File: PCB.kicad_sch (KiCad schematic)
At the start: 17 parts, among them J1 Conector IR, J10 Conector ultrassonico esquerdo, J11 Conector ultrassonico central, J12 Conector ultrassonico direito, J13 Conector LED Extra, J14 Conector LORA, J15 ENCO_SW_Esq, J16 ENCO_SW_Dir, J2 Conector bluetooth, J3 Conector Acelerometro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

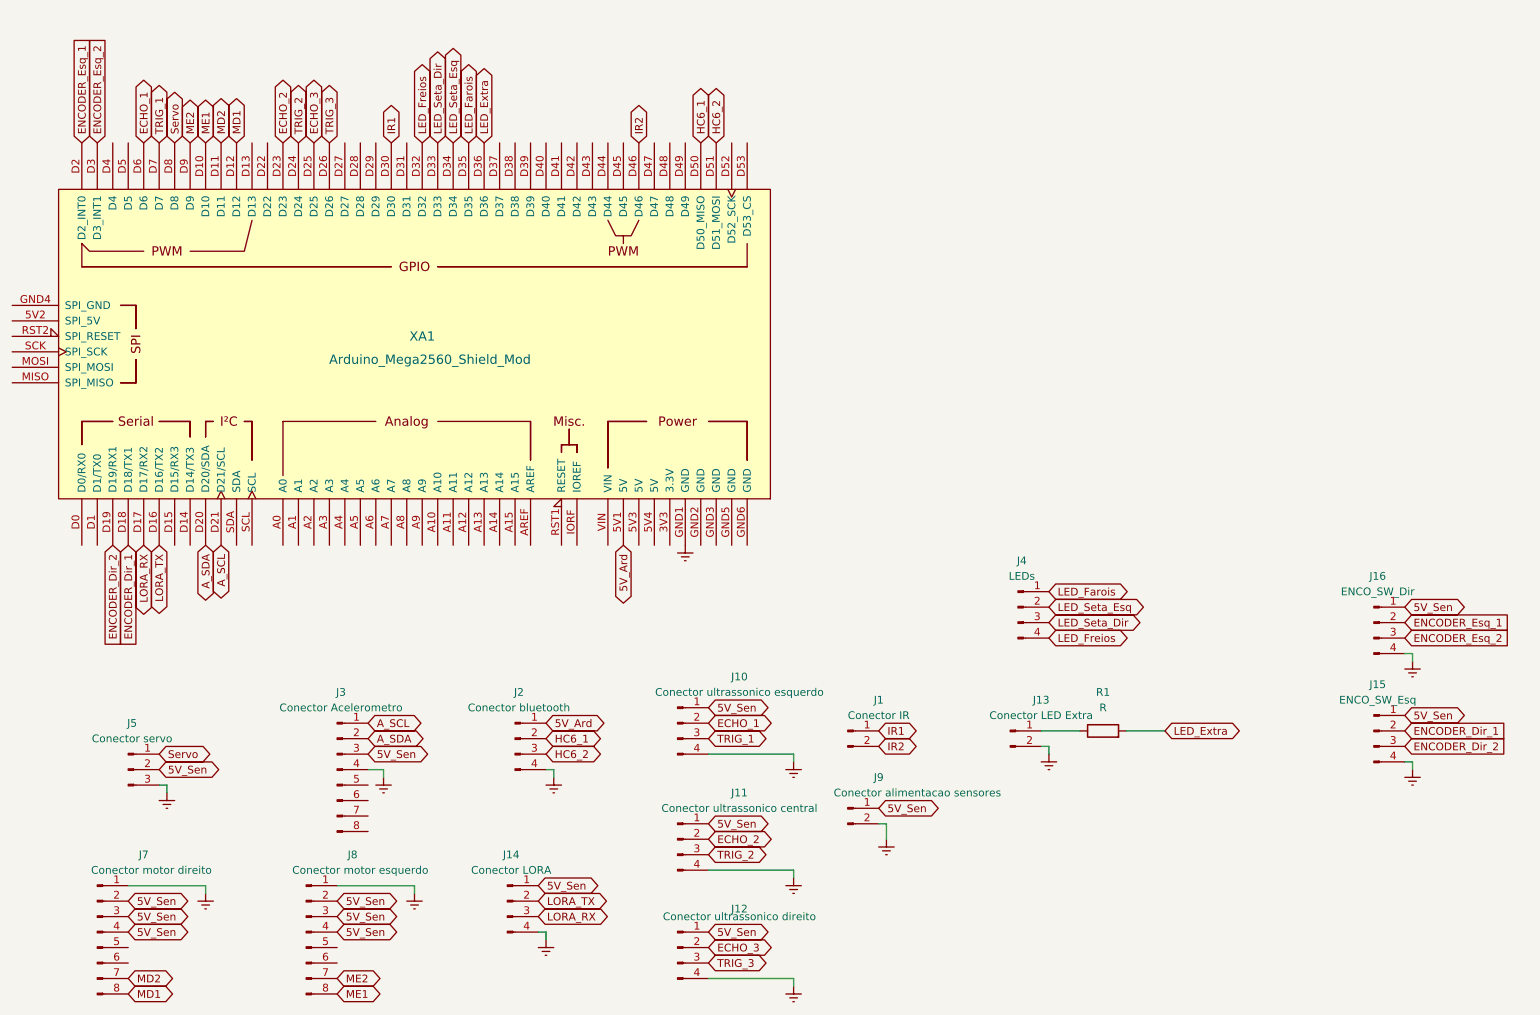
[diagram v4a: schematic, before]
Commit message: fix: adição da entrada 8.4V do servo e outros
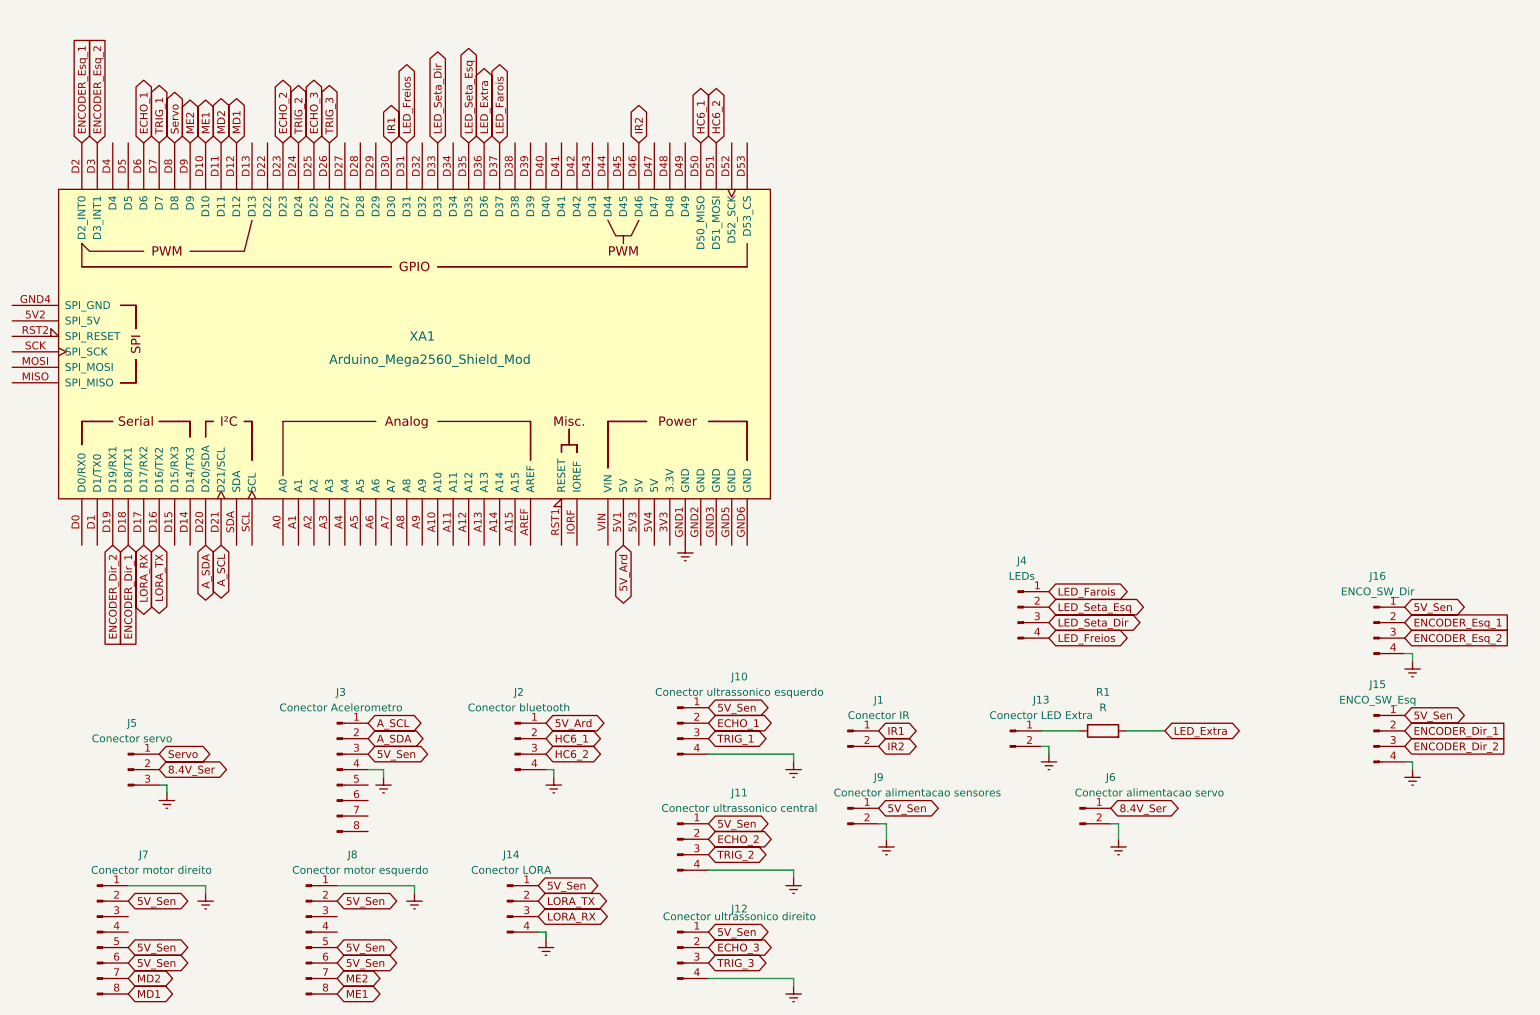
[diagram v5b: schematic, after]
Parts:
- added J6: Conector alimentacao servo, TerminalBlock_Phoenix:TerminalBlock_Phoenix_MKDS-1,5-2_1x02_P5.00mm_Horizontal, symbol Connector:Conn_01x02_Pin
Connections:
- net 5V_Sen: now also J7.5 (Pin_5), J7.6 (Pin_6), J8.5 (Pin_5), J8.6 (Pin_6); no longer J5.2 (Pin_2), J7.3 (Pin_3), J7.4 (Pin_4), J8.3 (Pin_3), J8.4 (Pin_4)
- net Earth: now also J6.2 (Pin_2)
- net LED_Farois: now also XA1.D37; no longer XA1.D35
- net LED_Freios: now also XA1.D31; no longer XA1.D32
- net LED_Seta_Esq: now also XA1.D35; no longer XA1.D34
- new net 8.4V_Ser: J5.2 (Pin_2), J6.1 (Pin_1)
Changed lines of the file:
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@@
 (kicad_sch (version 20230121) (generator eeschema)
   (paper "A4")
+  (wire (pts (xy 205.74 158.75) (xy 205.74 161.29))
+    (stroke (width 0) (type default))
+  )
   (wire (pts (xy 77.47 168.91) (xy 90.17 168.91))
     (stroke (width 0) (type default))
@@
   )
   (wire (pts (xy 138.43 184.15) (xy 152.4 184.15))
+    (stroke (width 0) (type default))
+  )
+  (wire (pts (xy 204.47 158.75) (xy 205.74 158.75))
     (stroke (width 0) (type default))
   )
@@
     )
   )
+  (global_label "LED_Seta_Esq" (shape bidirectional) (at 99.06 46.99 90) (fields_autoplaced)
+    (effects (font (size 1.27 1.27)) (justify left))
+    (property "Intersheetrefs" "${INTERSHEET_REFS}" (at 99.06 30.0123 90)
+      (effects (font (size 1.27 1.27)) (justify left) hide)
+    )
+  )
   (global_label "5V_Sen" (shape bidirectional) (at 138.43 139.7 0) (fields_autoplaced)
     (effects (font (size 1.27 1.27)) (justify left))
@@
     )
   )
-  (global_label "5V_Sen" (shape bidirectional) (at 43.18 173.99 0) (fields_autoplaced)
-    (effects (font (size 1.27 1.27)) (justify left))
-    (property "Intersheetrefs" "${INTERSHEET_REFS}" (at 53.9893 173.99 0)
-      (effects (font (size 1.27 1.27)) (justify left) hide)
-    )
-  )
   (global_label "ECHO_1" (shape bidirectional) (at 45.72 46.99 90) (fields_autoplaced)
     (effects (font (size 1.27 1.27)) (justify left))
@@
     )
   )
-  (global_label "LED_Extra" (shape bidirectional) (at 101.6 46.99 90) (fields_autoplaced)
-    (effects (font (size 1.27 1.27)) (justify left))
-    (property "Intersheetrefs" "${INTERSHEET_REFS}" (at 101.6 33.6408 90)
-      (effects (font (size 1.27 1.27)) (justify left) hide)
-    )
-  )
   (global_label "LED_Seta_Dir" (shape bidirectional) (at 93.98 46.99 90) (fields_autoplaced)
     (effects (font (size 1.27 1.27)) (justify left))
@@
     )
   )
-  (global_label "5V_Sen" (shape bidirectional) (at 48.26 149.86 0) (fields_autoplaced)
-    (effects (font (size 1.27 1.27)) (justify left))
-    (property "Intersheetrefs" "${INTERSHEET_REFS}" (at 59.0693 149.86 0)
+  (global_label "8.4V_Ser" (shape bidirectional) (at 48.26 149.86 0) (fields_autoplaced)
+    (effects (font (size 1.27 1.27)) (justify left))
+    (property "Intersheetrefs" "${INTERSHEET_REFS}" (at 60.5208 149.86 0)
       (effects (font (size 1.27 1.27)) (justify left) hide)
     )
@@
     (effects (font (size 1.27 1.27)) (justify left))
     (property "Intersheetrefs" "${INTERSHEET_REFS}" (at 121.2993 168.91 0)
-      (effects (font (size 1.27 1.27)) (justify left) hide)
-    )
-  )
-  (global_label "5V_Sen" (shape bidirectional) (at 77.47 176.53 0) (fields_autoplaced)
-    (effects (font (size 1.27 1.27)) (justify left))
-    (property "Intersheetrefs" "${INTERSHEET_REFS}" (at 88.2793 176.53 0)
       (effects (font (size 1.27 1.27)) (justify left) hide)
     )
@@
     )
   )
-  (global_label "LED_Freios" (shape bidirectional) (at 91.44 46.99 90) (fields_autoplaced)
-    (effects (font (size 1.27 1.27)) (justify left))
-    (property "Intersheetrefs" "${INTERSHEET_REFS}" (at 91.44 32.7335 90)
+  (global_label "LED_Freios" (shape bidirectional) (at 88.9 46.99 90) (fields_autoplaced)
+    (effects (font (size 1.27 1.27)) (justify left))
+    (property "Intersheetrefs" "${INTERSHEET_REFS}" (at 88.9 32.7335 90)
+      (effects (font (size 1.27 1.27)) (justify left) hide)
+    )
+  )
+  (global_label "5V_Sen" (shape bidirectional) (at 43.18 181.61 0) (fields_autoplaced)
+    (effects (font (size 1.27 1.27)) (justify left))
+    (property "Intersheetrefs" "${INTERSHEET_REFS}" (at 53.9893 181.61 0)
+      (effects (font (size 1.27 1.27)) (justify left) hide)
+    )
+  )
+  (global_label "5V_Sen" (shape bidirectional) (at 77.47 181.61 0) (fields_autoplaced)
+    (effects (font (size 1.27 1.27)) (justify left))
+    (property "Intersheetrefs" "${INTERSHEET_REFS}" (at 88.2793 181.61 0)
       (effects (font (size 1.27 1.27)) (justify left) hide)
     )
@@
     )
   )
-  (global_label "LED_Seta_Esq" (shape bidirectional) (at 96.52 46.99 90) (fields_autoplaced)
-    (effects (font (size 1.27 1.27)) (justify left))
-    (property "Intersheetrefs" "${INTERSHEET_REFS}" (at 96.52 30.0123 90)
-      (effects (font (size 1.27 1.27)) (justify left) hide)
-    )
-  )
   (global_label "ECHO_3" (shape bidirectional) (at 73.66 46.99 90) (fields_autoplaced)
     (effects (font (size 1.27 1.27)) (justify left))
@@
     )
   )
+  (global_label "8.4V_Ser" (shape bidirectional) (at 204.47 156.21 0) (fields_autoplaced)
+    (effects (font (size 1.27 1.27)) (justify left))
+    (property "Intersheetrefs" "${INTERSHEET_REFS}" (at 216.7308 156.21 0)
+      (effects (font (size 1.27 1.27)) (justify left) hide)
+    )
+  )
   (global_label "ECHO_2" (shape bidirectional) (at 138.43 161.29 0) (fields_autoplaced)
     (effects (font (size 1.27 1.27)) (justify left))
@@
     )
   )
+  (global_label "LED_Farois" (shape bidirectional) (at 104.14 46.99 90) (fields_autoplaced)
+    (effects (font (size 1.27 1.27)) (justify left))
+    (property "Intersheetrefs" "${INTERSHEET_REFS}" (at 104.14 32.6731 90)
+      (effects (font (size 1.27 1.27)) (justify left) hide)
+    )
+  )
   (global_label "5V_Sen" (shape bidirectional) (at 43.18 171.45 0) (fields_autoplaced)
     (effects (font (size 1.27 1.27)) (justify left))
@@
     (effects (font (size 1.27 1.27)) (justify left))
     (property "Intersheetrefs" "${INTERSHEET_REFS}" (at 127 39.8092 90)
+      (effects (font (size 1.27 1.27)) (justify left) hide)
+    )
+  )
+  (global_label "LED_Extra" (shape bidirectional) (at 101.6 46.99 90) (fields_autoplaced)
+    (effects (font (size 1.27 1.27)) (justify left))
+    (property "Intersheetrefs" "${INTERSHEET_REFS}" (at 101.6 33.6408 90)
       (effects (font (size 1.27 1.27)) (justify left) hide)
     )
@@
     )
   )
-  (global_label "5V_Sen" (shape bidirectional) (at 43.18 176.53 0) (fields_autoplaced)
-    (effects (font (size 1.27 1.27)) (justify left))
-    (property "Intersheetrefs" "${INTERSHEET_REFS}" (at 53.9893 176.53 0)
-      (effects (font (size 1.27 1.27)) (justify left) hide)
-    )
-  )
   (global_label "A_SDA" (shape bidirectional) (at 82.55 144.78 0) (fields_autoplaced)
     (effects (font (size 1.27 1.27)) (justify left))
@@
     (effects (font (size 1.27 1.27)) (justify left))
     (property "Intersheetrefs" "${INTERSHEET_REFS}" (at 85.3764 184.15 0)
+      (effects (font (size 1.27 1.27)) (justify left) hide)
+    )
+  )
+  (global_label "5V_Sen" (shape bidirectional) (at 77.47 179.07 0) (fields_autoplaced)
+    (effects (font (size 1.27 1.27)) (justify left))
+    (property "Intersheetrefs" "${INTERSHEET_REFS}" (at 88.2793 179.07 0)
       (effects (font (size 1.27 1.27)) (justify left) hide)
     )
@@
     )
   )
-  (global_label "5V_Sen" (shape bidirectional) (at 77.47 173.99 0) (fields_autoplaced)
-    (effects (font (size 1.27 1.27)) (justify left))
-    (property "Intersheetrefs" "${INTERSHEET_REFS}" (at 88.2793 173.99 0)
-      (effects (font (size 1.27 1.27)) (justify left) hide)
-    )
-  )
   (global_label "MD2" (shape bidirectional) (at 43.18 184.15 0) (fields_autoplaced)
     (effects (font (size 1.27 1.27)) (justify left))
@@
     )
   )
-  (global_label "LED_Farois" (shape bidirectional) (at 99.06 46.99 90) (fields_autoplaced)
-    (effects (font (size 1.27 1.27)) (justify left))
-    (property "Intersheetrefs" "${INTERSHEET_REFS}" (at 99.06 32.6731 90)
-      (effects (font (size 1.27 1.27)) (justify left) hide)
-    )
-  )
   (global_label "HC6_2" (shape bidirectional) (at 139.7 46.99 90) (fields_autoplaced)
     (effects (font (size 1.27 1.27)) (justify left))
     (property "Intersheetrefs" "${INTERSHEET_REFS}" (at 139.7 36.9064 90)
+      (effects (font (size 1.27 1.27)) (justify left) hide)
+    )
+  )
+  (global_label "5V_Sen" (shape bidirectional) (at 43.18 179.07 0) (fields_autoplaced)
+    (effects (font (size 1.27 1.27)) (justify left))
+    (property "Intersheetrefs" "${INTERSHEET_REFS}" (at 53.9893 179.07 0)
       (effects (font (size 1.27 1.27)) (justify left) hide)
     )
@@
     )
   )
+  (symbol (lib_id "Connector:Conn_01x02_Pin") (at 199.39 156.21 0) (unit 1)
+    (in_bom yes) (on_board yes) (dnp no)
+    (property "Reference" "J6" (at 204.47 151.13 0)
+      (effects (font (size 1.27 1.27)))
+    )
+    (property "Value" "Conector alimentacao servo" (at 210.82 153.67 0)
+      (effects (font (size 1.27 1.27)))
+    )
+    (property "Footprint" "TerminalBlock_Phoenix:TerminalBlock_Phoenix_MKDS-1,5-2_1x02_P5.00mm_Horizontal" (at 199.39 156.21 0)
+      (effects (font (size 1.27 1.27)) hide)
+    )
+    (property "Datasheet" "~" (at 199.39 156.21 0)
+      (effects (font (size 1.27 1.27)) hide)
+    )
+    (pin "1")
+    (pin "2")
+    (instances
+      (project "PCB"
+        (path "/b344186f-9059-49c5-a6f7-f90c862ad97f"
+          (reference "J6") (unit 1)
+        )
+      )
+    )
+  )
   (symbol (lib_id "Connector:Conn_01x08_Pin") (at 38.1 176.53 0) (unit 1)
     (in_bom yes) (on_board yes) (dnp no)
@@
         )
       )
+    )
+  )
+  (symbol (lib_id "power:Earth") (at 205.74 161.29 0) (unit 1)
+    (in_bom yes) (on_board yes) (dnp no) (fields_autoplaced)
+    (property "Reference" "#PWR015" (at 205.74 167.64 0)
+      (effects (font (size 1.27 1.27)) hide)
+    )
+    (property "Value" "Earth" (at 205.74 165.1 0)
+      (effects (font (size 1.27 1.27)) hide)
+    )
+    (property "Footprint" "" (at 205.74 161.29 0)
+      (effects (font (size 1.27 1.27)) hide)
+    )
+    (property "Datasheet" "~" (at 205.74 161.29 0)
+      (effects (font (size 1.27 1.27)) hide)
+    )
+    (pin "1")
+    (instances
+      (project "PCB"
+        (path "/b344186f-9059-49c5-a6f7-f90c862ad97f"
+          (reference "#PWR015") (unit 1)
+        )
+      )
+      (project "esquemaEletricoCarro"
+        (path "/e63e39d7-6ac0-4ffd-8aa3-1841a4541b55/ef1da815-5ae9-4f7a-859c-d7960e6acc1e"
+          (reference "#PWR021") (unit 1)
+        )
+      )
